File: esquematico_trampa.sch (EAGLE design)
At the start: 17 parts, among them U1 MICROCHIP_MCP3008-I-PMICROCHI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, U2 LM358PE3

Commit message: Nombre todas las pistas dependiendo su conexión
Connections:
- net N$1 renamed SW12V
- net N$2 renamed 1N+
- net N$3 renamed V_49E
- net N$4 renamed V_LM35
- net N$6 renamed 1N-
- net N$7 renamed 2N+
- net N$9 renamed 2N-
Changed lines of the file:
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@@
 </segment>
 </net>
-<net name="N$3" class="0">
+<net name="V_49E" class="0">
 <segment>
 <pinref part="49E_PIN" gate="-3" pin="S"/>
@@
 <pinref part="U1" gate="G$0" pin="CH3"/>
 <wire x1="101.6" y1="58.42" x2="93.98" y2="58.42" width="0.1524" layer="91"/>
+<label x="81.28" y="55.88" size="1.778" layer="95"/>
 </segment>
 </net>
-<net name="N$4" class="0">
+<net name="V_LM35" class="0">
 <segment>
 <pinref part="LM35_PIN" gate="-2" pin="S"/>
@@
 <pinref part="U1" gate="G$0" pin="CH0"/>
 <wire x1="60.96" y1="66.04" x2="101.6" y2="66.04" width="0.1524" layer="91"/>
+<label x="81.28" y="66.04" size="1.778" layer="95"/>
 </segment>
 </net>
-<net name="N$2" class="0">
+<net name="1N+" class="0">
 <segment>
 <pinref part="SCT013_20A_PIN" gate="-1" pin="S"/>
@@
 <wire x1="-15.24" y1="22.86" x2="25.4" y2="22.86" width="0.1524" layer="91"/>
 <wire x1="25.4" y1="22.86" x2="25.4" y2="15.24" width="0.1524" layer="91"/>
+<label x="10.16" y="22.86" size="1.778" layer="95"/>
 </segment>
 </net>
-<net name="N$6" class="0">
+<net name="1N-" class="0">
 <segment>
 <pinref part="U2" gate="G$1" pin="1IN-"/>
@@
 <wire x1="73.66" y1="63.5" x2="73.66" y2="15.24" width="0.1524" layer="91"/>
 <junction x="73.66" y="15.24"/>
+<label x="20.32" y="12.7" size="1.778" layer="95"/>
 </segment>
 </net>
-<net name="N$7" class="0">
+<net name="2N+" class="0">
 <segment>
 <pinref part="SCT013_100A_PIN" gate="-1" pin="S"/>
@@
 <pinref part="U2" gate="G$1" pin="2IN+"/>
 <wire x1="22.86" y1="10.16" x2="25.4" y2="10.16" width="0.1524" layer="91"/>
+<label x="7.62" y="2.54" size="1.778" layer="95"/>
 </segment>
 </net>
-<net name="N$9" class="0">
+<net name="2N-" class="0">
 <segment>
 <pinref part="U2" gate="G$1" pin="2IN-"/>
@@
 <wire x1="78.74" y1="12.7" x2="66.04" y2="12.7" width="0.1524" layer="91"/>
 <junction x="66.04" y="12.7"/>
+<label x="22.86" y="-2.54" size="1.778" layer="95"/>
 </segment>
 </net>
@@
 </segment>
 </net>
-<net name="N$1" class="0">
+<net name="SW12V" class="0">
 <segment>
 <pinref part="VCC" gate="-1" pin="KL"/>
@@
 <pinref part="12V" gate="-1" pin="S"/>
 <wire x1="20.32" y1="127" x2="30.48" y2="127" width="0.1524" layer="91"/>
+<label x="20.32" y="149.86" size="1.778" layer="95"/>
 </segment>
 </net>

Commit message: Esquemático más optimizado
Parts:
- renumbered GPIO_RASPBERRY to RASPBERRY
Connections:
- net 2A renamed N$3
- net 2B renamed N$4
- net SW12V renamed N$5
- net V_LM35 renamed N$10
- removed net 1A: A4988.1A, M-1.S
- removed net 1B: A4988.1B, M-2.S
- removed net 1N+: SCT013_20A_PIN-1.S, U2.1IN+
- removed net 1N-: U1.CH1, U2.1IN-, U2.1OUT
- removed net 2N+: SCT013_100A_PIN-1.S, U2.2IN+
- removed net 2N-: U1.CH2, U2.2IN-, U2.2OUT
- removed net 3V3: RASPBERRY.17
- removed net 5VV: RASPBERRY.4
- removed net GPIO12: RASPBERRY.32
- removed net GPIO14: RASPBERRY.8
- removed net GPIO15: RASPBERRY.10
- removed net GPIO17: RASPBERRY.11
- removed net GPIO18: RASPBERRY.12
- removed net GPIO22: A4988.STEP, RASPBERRY.15
- removed net GPIO23: DHT11_PIN-2.S, RASPBERRY.16
- removed net GPIO24: A4988.!ENABLE, RASPBERRY.18
- removed net GPIO25: RASPBERRY.22
- removed net GPIO27: A4988.DIR, RASPBERRY.13
- removed net GPIO4: RASPBERRY.7
- removed net IN12+: 12V-2.S, A4988.VMOT, REG.2
- removed net NULL: RASPBERRY.27, RASPBERRY.28
- removed net OUT5+: REG.1, VCCRB-1.KL
- removed net OUTGND: REG.3, VCCRB-2.KL
- removed net SPICEO1: RASPBERRY.26
- removed net V_49E: 49E_PIN-3.S, U1.CH3
- new net N$1: A4988.1B, M-1.S
- new net N$11: U1.CH2, U2.1IN-, U2.1OUT
- new net N$12: U1.CH3, U2.2IN-, U2.2OUT
- new net N$13: 49E_PIN-3.S, U1.CH1
- new net N$14: SCT013_100A_PIN-1.S, U2.1IN+
- new net N$16: SCT013_20A_PIN-1.S, U2.2IN+
- new net N$2: A4988.1A, M-2.S
- new net N$6: 12V-2.S, A4988.VMOT, REG.1
- new net N$7: REG.3, VCC-2.KL
- new net N$8: A4988.VDD, REG.2, VCCRB-1.KL
- new net N$9: REG.4, VCCRB-2.KL
- net 5V: no longer A4988.VDD
- net GND: no longer RASPBERRY.14, RASPBERRY.20, RASPBERRY.30, RASPBERRY.34, RASPBERRY.9, REG.4, VCC-2.KL
- net GPIO13: now also A4988.!SLEEP
- net GPIO16: now also SCR40_2-1.S
- net GPIO19: now also A4988.STEP
- net GPIO21: now also DHT11_PIN-2.S; no longer SCR40_2-1.S
- net GPIO26: now also A4988.DIR
- net GPIO5: now also A4988.!ENABLE; no longer A4988.!SLEEP
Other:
- moved on the sheet: 12V-1, 12V-2, 49E_PIN-1, 49E_PIN-2, 49E_PIN-3, A4988, BMP_PIN-1, BMP_PIN-2, BMP_PIN-3, BMP_PIN-4, DHT11_PIN-1, DHT11_PIN-2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

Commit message: Renombre todas las conexiones
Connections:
- net N$1 renamed 1B
- net N$10 renamed V_LM35
- net N$11 renamed V_SCT100
- net N$12 renamed V_SCT20
- net N$13 renamed V_49E
- net N$14 renamed OUT_SCT100
- net N$16 renamed OUT_SCT20
- net N$2 renamed 1A
- net N$3 renamed 2A
- net N$4 renamed 2B
- net N$5 renamed 12+
- net N$6 renamed SW12
- net N$8 renamed IN5+
- removed net N$7: REG.3, VCC-2.KL
- removed net N$9: REG.4, VCCRB-2.KL
- net GND: now also REG.3, REG.4, VCC-2.KL, VCCRB-2.KL
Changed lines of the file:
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@@
 </variantdefs>
 <classes>
-<class number="0" name="default" width="0" drill="0">
+<class number="0" name="Raspberry gpio" width="0.508" drill="0.254">
+<clearance class="0" value="0.254"/>
+</class>
+<class number="1" name="VCC " width="0" drill="0">
 </class>
 </classes>
@@
 <net name="GND" class="0">
 <segment>
-<pinref part="RASPBERRY" gate="A" pin="25"/>
-<label x="86.36" y="132.08" size="1.778" layer="95" grouprefs="GPIO_RASPBERRY"/>
-<wire x1="99.06" y1="132.08" x2="66.04" y2="132.08" width="0.1524" layer="91"/>
-<wire x1="66.04" y1="132.08" x2="66.04" y2="144.78" width="0.1524" layer="91"/>
-<wire x1="66.04" y1="144.78" x2="38.1" y2="144.78" width="0.1524" layer="91"/>
-<pinref part="U1" gate="G$0" pin="DGND"/>
-<wire x1="38.1" y1="144.78" x2="38.1" y2="170.18" width="0.1524" layer="91"/>
-<wire x1="38.1" y1="170.18" x2="38.1" y2="175.26" width="0.1524" layer="91"/>
-<wire x1="38.1" y1="175.26" x2="38.1" y2="180.34" width="0.1524" layer="91"/>
-<wire x1="38.1" y1="180.34" x2="40.64" y2="180.34" width="0.1524" layer="91"/>
-<pinref part="U1" gate="G$0" pin="AGND"/>
-<wire x1="40.64" y1="175.26" x2="38.1" y2="175.26" width="0.1524" layer="91"/>
-<junction x="38.1" y="175.26"/>
-<pinref part="BMP_PIN" gate="-2" pin="S"/>
-<wire x1="58.42" y1="154.94" x2="63.5" y2="154.94" width="0.1524" layer="91"/>
-<wire x1="63.5" y1="154.94" x2="63.5" y2="170.18" width="0.1524" layer="91"/>
-<wire x1="63.5" y1="170.18" x2="38.1" y2="170.18" width="0.1524" layer="91"/>
-<junction x="38.1" y="170.18"/>
-</segment>
-<segment>
 <pinref part="RASPBERRY" gate="A" pin="39"/>
 <wire x1="99.06" y1="114.3" x2="78.74" y2="114.3" width="0.1524" layer="91" grouprefs="GPIO_RASPBERRY"/>
@@
 <junction x="218.44" y="157.48"/>
 </segment>
+<segment>
+<pinref part="VCC" gate="-2" pin="KL"/>
+<wire x1="-33.02" y1="154.94" x2="-7.62" y2="154.94" width="0.1524" layer="91"/>
+<wire x1="-7.62" y1="154.94" x2="-7.62" y2="157.48" width="0.1524" layer="91"/>
+<pinref part="REG" gate="A" pin="3"/>
+<wire x1="-7.62" y1="157.48" x2="0" y2="157.48" width="0.1524" layer="91"/>
+<pinref part="RASPBERRY" gate="A" pin="25"/>
+<label x="86.36" y="132.08" size="1.778" layer="95" grouprefs="GPIO_RASPBERRY"/>
+<wire x1="99.06" y1="132.08" x2="66.04" y2="132.08" width="0.1524" layer="91"/>
+<wire x1="66.04" y1="132.08" x2="66.04" y2="144.78" width="0.1524" layer="91"/>
+<wire x1="66.04" y1="144.78" x2="38.1" y2="144.78" width="0.1524" layer="91"/>
+<pinref part="U1" gate="G$0" pin="DGND"/>
+<wire x1="38.1" y1="144.78" x2="38.1" y2="170.18" width="0.1524" layer="91"/>
+<wire x1="38.1" y1="170.18" x2="38.1" y2="175.26" width="0.1524" layer="91"/>
+<wire x1="38.1" y1="175.26" x2="38.1" y2="180.34" width="0.1524" layer="91"/>
+<wire x1="38.1" y1="180.34" x2="40.64" y2="180.34" width="0.1524" layer="91"/>
+<pinref part="U1" gate="G$0" pin="AGND"/>
+<wire x1="40.64" y1="175.26" x2="38.1" y2="175.26" width="0.1524" layer="91"/>
+<junction x="38.1" y="175.26"/>
+<pinref part="BMP_PIN" gate="-2" pin="S"/>
+<wire x1="58.42" y1="154.94" x2="63.5" y2="154.94" width="0.1524" layer="91"/>
+<wire x1="63.5" y1="154.94" x2="63.5" y2="170.18" width="0.1524" layer="91"/>
+<wire x1="63.5" y1="170.18" x2="38.1" y2="170.18" width="0.1524" layer="91"/>
+<junction x="38.1" y="170.18"/>
+<pinref part="REG" gate="A" pin="4"/>
+<wire x1="7.62" y1="157.48" x2="33.02" y2="157.48" width="0.1524" layer="91"/>
+<pinref part="VCCRB" gate="-2" pin="KL"/>
+<wire x1="33.02" y1="157.48" x2="33.02" y2="185.42" width="0.1524" layer="91"/>
+<wire x1="33.02" y1="185.42" x2="17.78" y2="185.42" width="0.1524" layer="91"/>
+<wire x1="33.02" y1="157.48" x2="33.02" y2="144.78" width="0.1524" layer="91"/>
+<junction x="33.02" y="157.48"/>
+<wire x1="33.02" y1="144.78" x2="38.1" y2="144.78" width="0.1524" layer="91"/>
+<junction x="38.1" y="144.78"/>
+<wire x1="-7.62" y1="154.94" x2="-7.62" y2="144.78" width="0.1524" layer="91"/>
+<wire x1="-7.62" y1="144.78" x2="33.02" y2="144.78" width="0.1524" layer="91"/>
+<junction x="-7.62" y="154.94"/>
+<junction x="33.02" y="144.78"/>
+</segment>
 </net>
 <net name="SPMOS1" class="0">
@@
 </segment>
 </net>
-<net name="N$1" class="0">
+<net name="1B" class="0">
 <segment>
 <pinref part="M" gate="-1" pin="S"/>
@@
 <pinref part="A4988" gate="G$1" pin="1B"/>
 <wire x1="27.94" y1="124.46" x2="33.02" y2="124.46" width="0.1524" layer="91"/>
-</segment>
-</net>
-<net name="N$2" class="0">
+<label x="27.94" y="124.46" size="1.778" layer="95"/>
+</segment>
+</net>
+<net name="1A" class="0">
 <segment>
 <pinref part="M" gate="-2" pin="S"/>
@@
 <pinref part="A4988" gate="G$1" pin="1A"/>
 <wire x1="30.48" y1="127" x2="33.02" y2="127" width="0.1524" layer="91"/>
-</segment>
-</net>
-<net name="N$3" class="0">
+<label x="27.94" y="129.54" size="1.778" layer="95"/>
+</segment>
+</net>
+<net name="2A" class="0">
 <segment>
 <pinref part="M" gate="-3" pin="S"/>
 <pinref part="A4988" gate="G$1" pin="2A"/>
 <wire x1="17.78" y1="121.92" x2="33.02" y2="121.92" width="0.1524" layer="91"/>
-</segment>
-</net>
-<net name="N$4" class="0">
+<label x="27.94" y="121.92" size="1.778" layer="95"/>
+</segment>
+</net>
+<net name="2B" class="0">
 <segment>
 <pinref part="M" gate="-4" pin="S"/>
 <pinref part="A4988" gate="G$1" pin="2B"/>
 <wire x1="17.78" y1="119.38" x2="33.02" y2="119.38" width="0.1524" layer="91"/>
-</segment>
-</net>
-<net name="N$5" class="0">
+<label x="27.94" y="119.38" size="1.778" layer="95"/>
+</segment>
+</net>
+<net name="12+" class="0">
 <segment>
 <pinref part="VCC" gate="-1" pin="KL"/>
@@
 <pinref part="12V" gate="-1" pin="S"/>
 <wire x1="-20.32" y1="160.02" x2="-20.32" y2="170.18" width="0.1524" layer="91"/>
-</segment>
-</net>
-<net name="N$6" class="0">
+<label x="-27.94" y="160.02" size="1.778" layer="95"/>
+</segment>
+</net>
+<net name="SW12" class="0">
 <segment>
 <pinref part="12V" gate="-2" pin="S"/>
@@
 <wire x1="-17.78" y1="149.86" x2="-17.78" y2="160.02" width="0.1524" layer="91"/>
 <junction x="-17.78" y="160.02"/>
-</segment>
-</net>
-<net name="N$7" class="0">
-<segment>
-<pinref part="VCC" gate="-2" pin="KL"/>
-<wire x1="-33.02" y1="154.94" x2="-7.62" y2="154.94" width="0.1524" layer="91"/>
-<wire x1="-7.62" y1="154.94" x2="-7.62" y2="157.48" width="0.1524" layer="91"/>
-<pinref part="REG" gate="A" pin="3"/>
-<wire x1="-7.62" y1="157.48" x2="0" y2="157.48" width="0.1524" layer="91"/>
-</segment>
-</net>
-<net name="N$8" class="0">
+<label x="-12.7" y="160.02" size="1.778" layer="95"/>
+</segment>
+</net>
+<net name="IN5+" class="0">
 <segment>
 <pinref part="REG" gate="A" pin="2"/>
@@
 <wire x1="27.94" y1="134.62" x2="27.94" y2="160.02" width="0.1524" layer="91"/>
 <junction x="27.94" y="160.02"/>
-</segment>
-</net>
-<net name="N$9" class="0">
-<segment>
-<pinref part="REG" gate="A" pin="4"/>
-<wire x1="7.62" y1="157.48" x2="33.02" y2="157.48" width="0.1524" layer="91"/>
-<pinref part="VCCRB" gate="-2" pin="KL"/>
-<wire x1="33.02" y1="157.48" x2="33.02" y2="185.42" width="0.1524" layer="91"/>
-<wire x1="33.02" y1="185.42" x2="17.78" y2="185.42" width="0.1524" layer="91"/>
-</segment>
-</net>
-<net name="N$10" class="0">
+<label x="20.32" y="160.02" size="1.778" layer="95"/>
+</segment>
+</net>
+<net name="V_LM35" class="0">
 <segment>
 <pinref part="U1" gate="G$0" pin="CH0"/>
@@
 <pinref part="LM35_PIN" gate="-2" pin="S"/>
 <wire x1="119.38" y1="223.52" x2="162.56" y2="223.52" width="0.1524" layer="91"/>
-</segment>
-</net>
-<net name="N$13" class="0">
+<label x="78.74" y="210.82" size="1.778" layer="95"/>
+</segment>
+</net>
+<net name="V_49E" class="0">
 <segment>
 <pinref part="49E_PIN" gate="-3" pin="S"/>
@@
 <pinref part="U1" gate="G$0" pin="CH1"/>
 <wire x1="81.28" y1="208.28" x2="68.58" y2="208.28" width="0.1524" layer="91"/>
-</segment>
-</net>
-<net name="N$11" class="0">
+<label x="88.9" y="203.2" size="1.778" layer="95"/>
+</segment>
+</net>
+<net name="V_SCT100" class="0">
 <segment>
 <pinref part="U2" gate="G$1" pin="1OUT"/>
@@
 <wire x1="170.18" y1="162.56" x2="170.18" y2="185.42" width="0.1524" layer="91"/>
 <junction x="170.18" y="185.42"/>
-</segment>
-</net>
-<net name="N$12" class="0">
+<label x="88.9" y="200.66" size="1.778" layer="95"/>
+</segment>
+</net>
+<net name="V_SCT20" class="0">
 <segment>
 <pinref part="U2" gate="G$1" pin="2OUT"/>
@@
 <wire x1="167.64" y1="160.02" x2="167.64" y2="182.88" width="0.1524" layer="91"/>
 <junction x="167.64" y="182.88"/>
-</segment>
-</net>
-<net name="N$14" class="0">
+<label x="88.9" y="195.58" size="1.778" layer="95"/>
+</segment>
+</net>
+<net name="OUT_SCT100" class="0">
 <segment>
 <pinref part="U2" gate="G$1" pin="1IN+"/>
@@
 <wire x1="208.28" y1="185.42" x2="208.28" y2="190.5" width="0.1524" layer="91"/>
 <wire x1="208.28" y1="190.5" x2="233.68" y2="190.5" width="0.1524" layer="91"/>
-</segment>
-</net>
-<net name="N$16" class="0">
+<label x="213.36" y="190.5" size="1.778" layer="95"/>
+</segment>
+</net>
+<net name="OUT_SCT20" class="0">
 <segment>
 <pinref part="U2" gate="G$1" pin="2IN+"/>
@@
 <pinref part="SCT013_20A_PIN" gate="-1" pin="S"/>
 <wire x1="223.52" y1="172.72" x2="233.68" y2="172.72" width="0.1524" layer="91"/>
-</segment>
-</net>
+<label x="213.36" y="180.34" size="1.778" layer="95"/>
+</segment>
+</net>

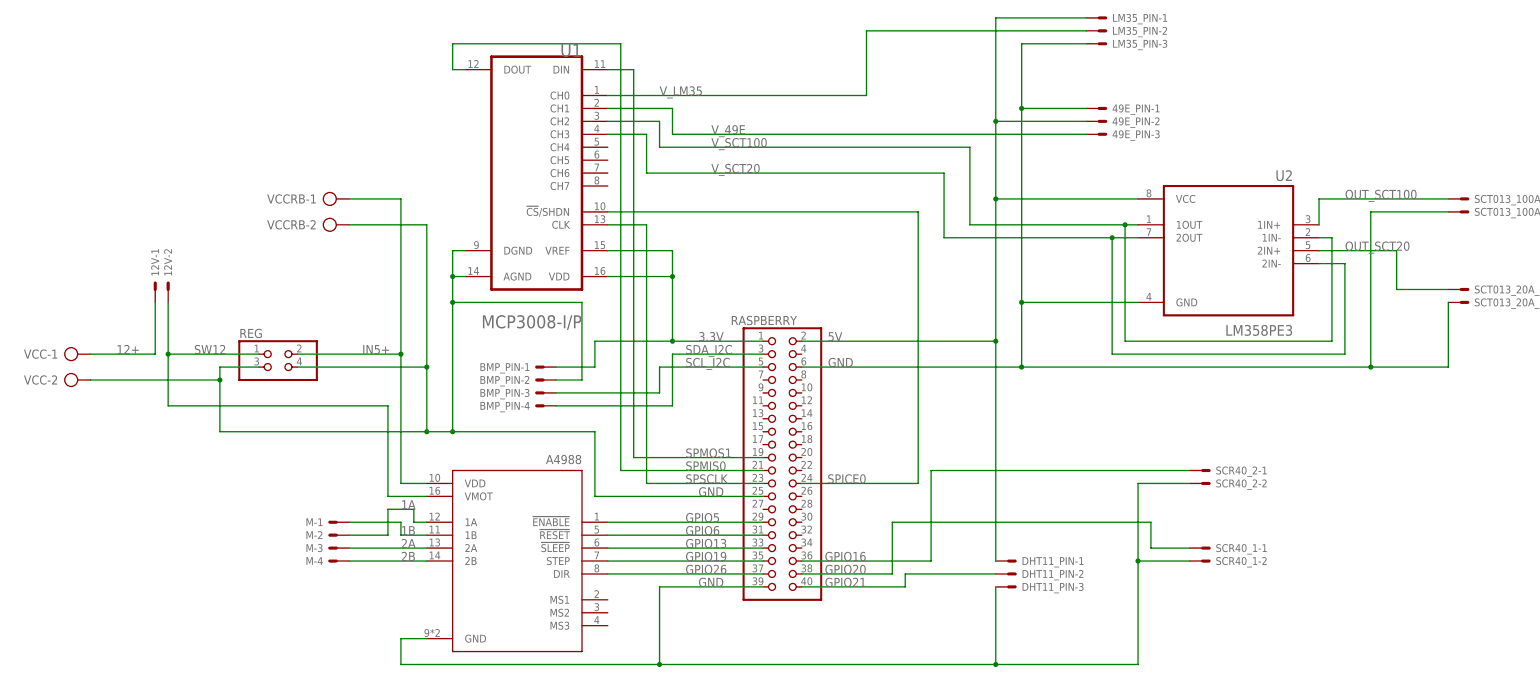
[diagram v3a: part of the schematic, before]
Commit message: agregue labels para evitar desorden en las conexiones
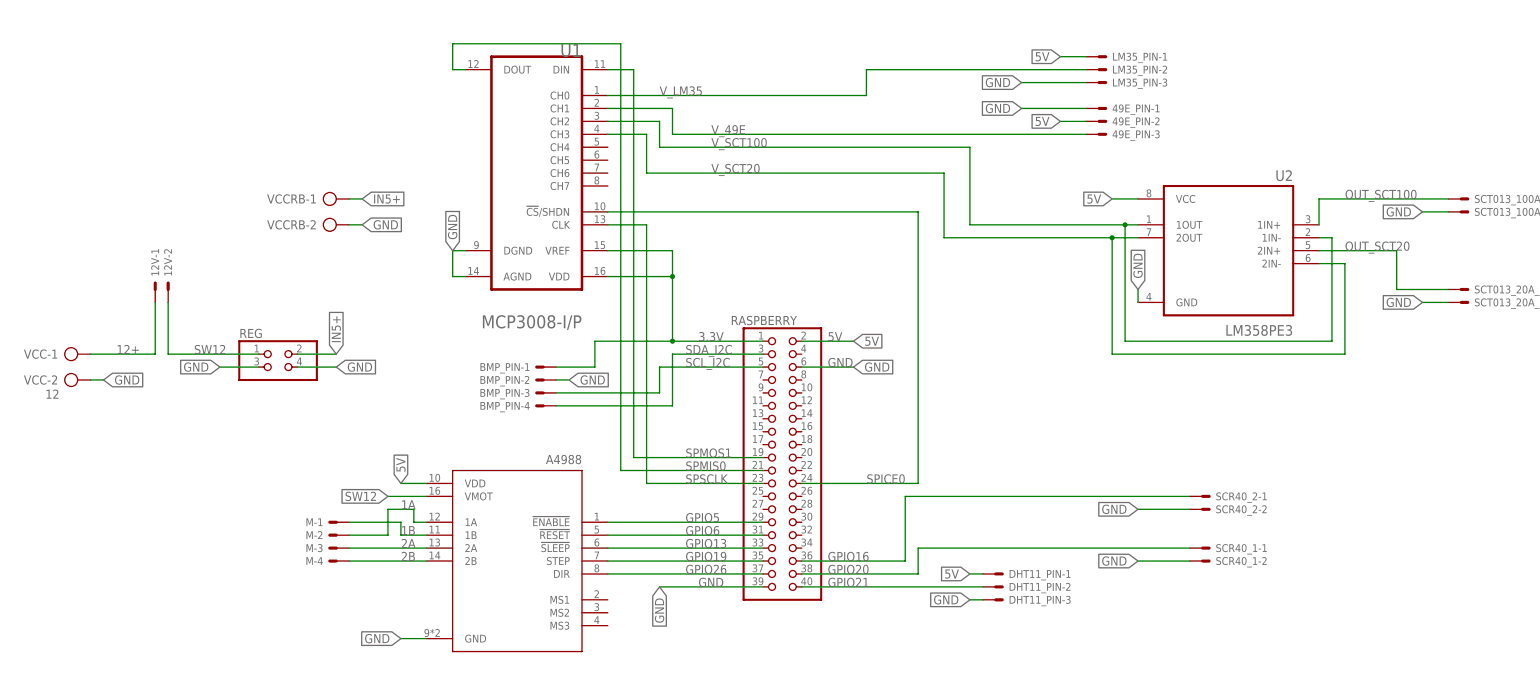
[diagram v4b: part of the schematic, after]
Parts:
- VCC: value (none) -> 12
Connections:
- net 5V: now also A4988.VDD
- net GND: no longer RASPBERRY.25
- net IN5+: no longer A4988.VDD
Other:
- moved on the sheet: DHT11_PIN-1, DHT11_PIN-2, DHT11_PIN-3, LM35_PIN-1, LM35_PIN-2, LM35_PIN-3, SCR40_2-1, SCR40_2-2
